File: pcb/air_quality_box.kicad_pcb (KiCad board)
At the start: 2 copper layers, 67.5 x 68 mm, 12 parts, among them J1 MH-Z19B, J2 BME680, J3 SPS30, J4 ST7565, SW1 SW_SPDT, U1 NodeMCU_ESP8266

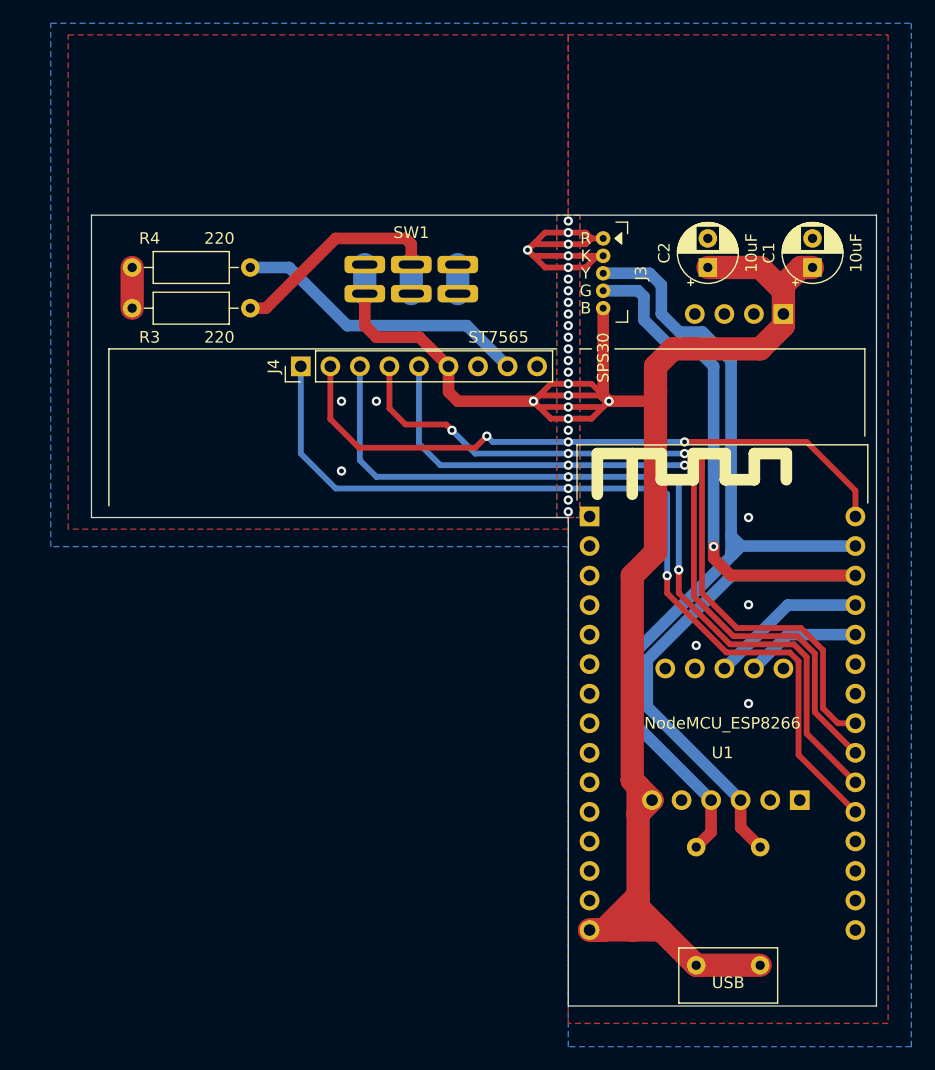
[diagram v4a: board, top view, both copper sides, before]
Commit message: Change route so that power lanes do not cross
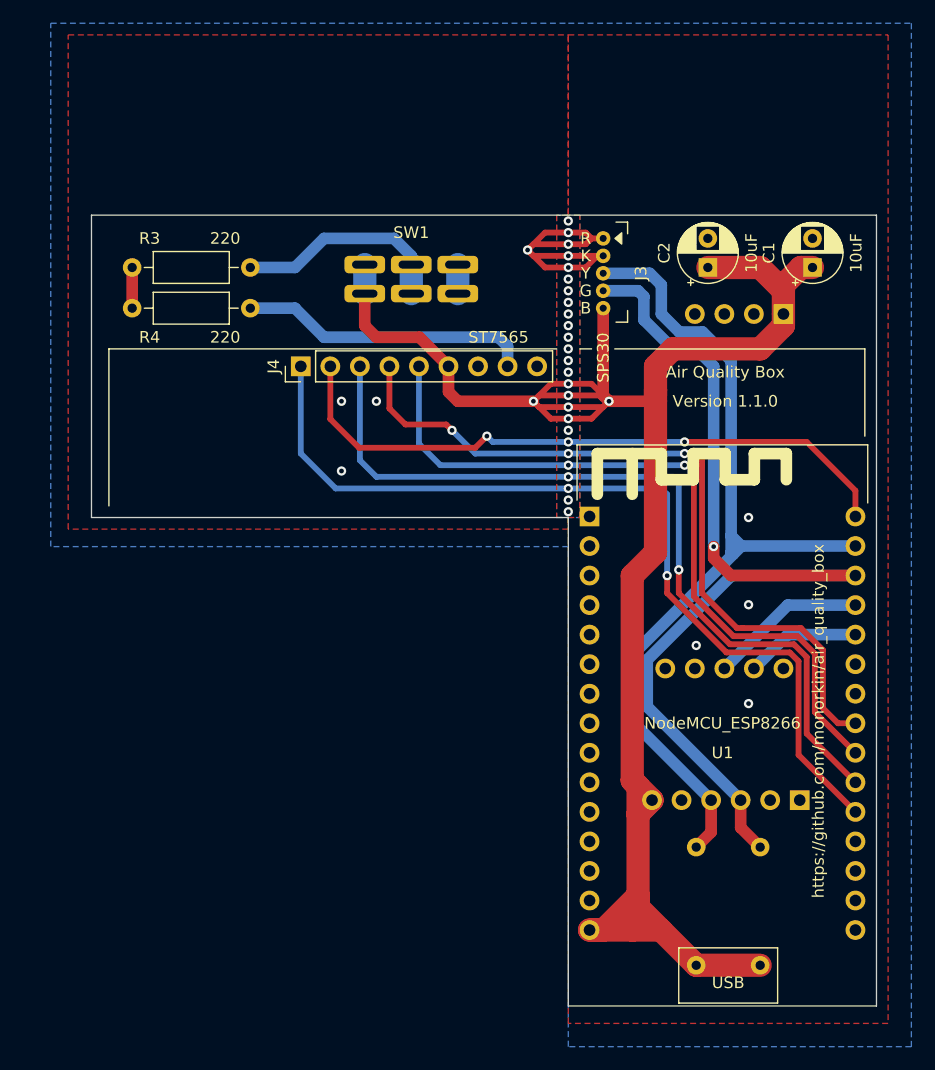
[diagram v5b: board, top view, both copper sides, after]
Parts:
- moved R3 3.50 mm to (102.0, 43.0)
- moved R4 3.50 mm to (112.2, 46.5)
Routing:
- net Net-(R3-Pad2): track 20.8 -> 18.7 mm
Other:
- board text added: "Air Quality Box"
- board text added: "Version 1.1.0"
- board text added: "https://github.com/monorkin/air_quality_box"
